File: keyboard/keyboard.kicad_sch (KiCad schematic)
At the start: 132 parts, among them SW1 MX_SW_HS, SW10 MX_SW_HS, SW11 MX_SW_HS, SW12 MX_SW_HS, SW13 MX_SW_HS, SW14 MX_SW_HS, SW15 MX_SW_HS, SW16 MX_SW_HS, SW17 MX_SW_HS, SW18 MX_SW_HS, SW19 MX_SW_HS, SW2 MX_SW_HS, SW20 MX_SW_HS, SW21 MX_SW_HS, SW22 MX_SW_HS, SW23 MX_SW_HS, SW24 MX_SW_HS, SW25 MX_SW_HS, SW26 MX_SW_HS, SW27 MX_SW_HS, SW28 MX_SW_HS, SW29 MX_SW_HS, SW3 MX_SW_HS, SW30 MX_SW_HS, SW31 MX_SW_HS, SW32 MX_SW_HS, SW33 MX_SW_HS, SW34 MX_SW_HS, SW35 MX_SW_HS, SW36 MX_SW_HS, SW37 MX_SW_HS, SW38 MX_SW_HS, SW39 MX_SW_HS, SW4 MX_SW_HS, SW40 MX_SW_HS, SW41 MX_SW_HS, SW42 MX_SW_HS, SW43 MX_SW_HS, SW44 MX_SW_HS, SW45 MX_SW_HS, SW46 MX_SW_HS, SW47 MX_SW_HS, SW48 MX_SW_HS, SW49 MX_SW_HS, SW5 MX_SW_HS, SW50 MX_SW_HS, SW51 MX_SW_HS, SW52 MX_SW_HS, SW53 MX_SW_HS, SW54 MX_SW_HS, SW55 MX_SW_HS, SW56 MX_SW_HS, SW57 MX_SW_HS, SW58 MX_SW_HS, SW59 MX_SW_HS, SW6 MX_SW_HS, SW60 MX_SW_HS, SW61 MX_SW_HS, SW62 MX_SW_HS, SW63 MX_SW_HS, SW64 MX_SW_HS, SW7 MX_SW_HS, SW8 MX_SW_HS, SW9 MX_SW_HS, U1 ProMicro

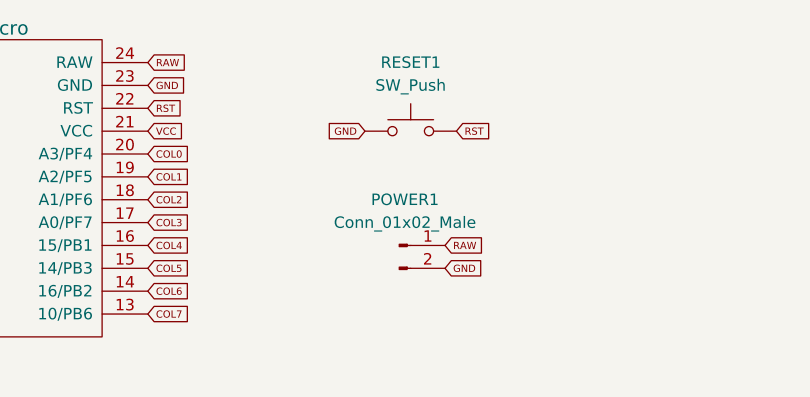
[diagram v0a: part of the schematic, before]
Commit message: Add the connector for the power switch and the holes for the broaching nuts
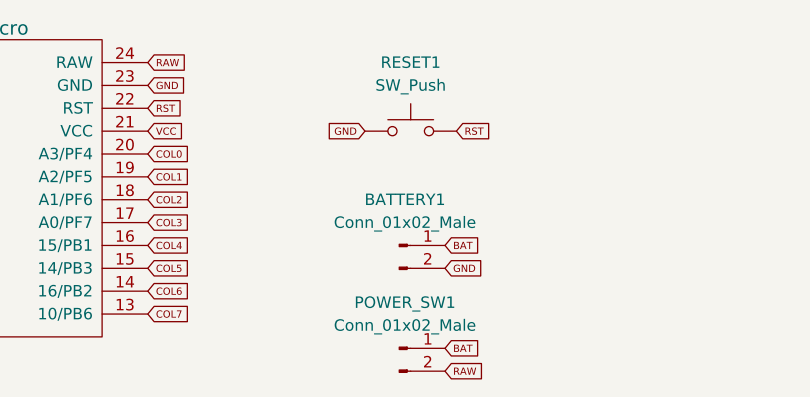
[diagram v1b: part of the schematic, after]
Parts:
- added POWER_SW1: Conn_01x02_Male, symbol Connector:Conn_01x02_Male
- renumbered POWER1 to BATTERY1
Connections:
- net RAW: now also POWER_SW1.2 (Pin_2); no longer BATTERY1.1 (Pin_1)
- new net BAT: BATTERY1.1 (Pin_1), POWER_SW1.1 (Pin_1)
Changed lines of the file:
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@@
+    )
+  )
+  (global_label "BAT" (shape input) (at 100.33 181.61 0) (fields_autoplaced)
+    (effects (font (size 0.8 0.8)) (justify left))
+    (property "Intersheet References" "${INTERSHEET_REFS}" (id 0) (at 103.9452 181.56 0)
+      (effects (font (size 0.8 0.8)) (justify left) hide)
     )
   )
@@
     )
   )
+  (global_label "RAW" (shape input) (at 100.33 184.15 0) (fields_autoplaced)
+    (effects (font (size 0.8 0.8)) (justify left))
+    (property "Intersheet References" "${INTERSHEET_REFS}" (id 0) (at 104.25 184.1 0)
+      (effects (font (size 0.8 0.8)) (justify left) hide)
+    )
+  )
   (global_label "ROW7" (shape input) (at 223.52 95.25 180) (fields_autoplaced)
     (effects (font (size 0.6 0.6)) (justify right))
@@
     )
   )
-  (global_label "RAW" (shape input) (at 100.33 170.18 0) (fields_autoplaced)
+  (global_label "BAT" (shape input) (at 100.33 170.18 0) (fields_autoplaced)
     (effects (font (size 0.8 0.8)) (justify left))
-    (property "Intersheet References" "${INTERSHEET_REFS}" (id 0) (at 104.25 170.13 0)
+    (property "Intersheet References" "${INTERSHEET_REFS}" (id 0) (at 103.9452 170.13 0)
       (effects (font (size 0.8 0.8)) (justify left) hide)
     )
@@
   (symbol (lib_id "Connector:Conn_01x02_Male") (at 95.25 170.18 0) (unit 1)
     (in_bom yes) (on_board yes) (fields_autoplaced)
-    (property "Reference" "POWER1" (id 0) (at 95.885 165.1 0))
+    (property "Reference" "BATTERY1" (id 0) (at 95.885 165.1 0))
     (property "Value" "Conn_01x02_Male" (id 1) (at 95.885 167.64 0))
     (property "Footprint" "" (id 2) (at 95.25 170.18 0)
@@
     (pin "2")
   )
+  (symbol (lib_id "Connector:Conn_01x02_Male") (at 95.25 181.61 0) (unit 1)
+    (in_bom yes) (on_board yes) (fields_autoplaced)
+    (property "Reference" "POWER_SW1" (id 0) (at 95.885 176.53 0))
+    (property "Value" "Conn_01x02_Male" (id 1) (at 95.885 179.07 0))
+    (property "Footprint" "" (id 2) (at 95.25 181.61 0)
+      (effects (font (size 1.27 1.27)) hide)
+    )
+    (property "Datasheet" "~" (id 3) (at 95.25 181.61 0)
+      (effects (font (size 1.27 1.27)) hide)
+    )
+    (pin "1")
+    (pin "2")
+  )
   (symbol (lib_id "Diode:1N4148") (at 76.2 95.25 0) (unit 1)
     (in_bom yes) (on_board yes) (fields_autoplaced)
@@
   )
   (symbol_instances
+    (path "/0ea7d412-6277-4227-b71e-6e4e29ffda6b"
+      (reference "BATTERY1") (unit 1) (value "Conn_01x02_Male") (footprint "Connector_PinHeader_2.54mm:PinHeader_1x02_P2.54mm_Vertical")
+    )
     (path "/6e969bfa-28c9-4212-88d0-f22e18a188be"
       (reference "D1") (unit 1) (value "1N4148") (footprint "Diode_THT:D_DO-35_SOD27_P7.62mm_Horizontal")
@@
       (reference "D64") (unit 1) (value "1N4148") (footprint "Diode_THT:D_DO-35_SOD27_P7.62mm_Horizontal")
     )
-    (path "/0ea7d412-6277-4227-b71e-6e4e29ffda6b"
-      (reference "POWER1") (unit 1) (value "Conn_01x02_Male") (footprint "Connector_PinHeader_2.54mm:PinHeader_1x02_P2.54mm_Vertical")
+    (path "/eda49190-6b3d-4bb1-b40a-0d620c2aa1aa"
+      (reference "POWER_SW1") (unit 1) (value "Conn_01x02_Male") (footprint "Connector_PinHeader_2.54mm:PinHeader_1x02_P2.54mm_Horizontal")
     )
     (path "/69aaefbf-88d4-415d-ad96-2a6ff3ee3a2f"

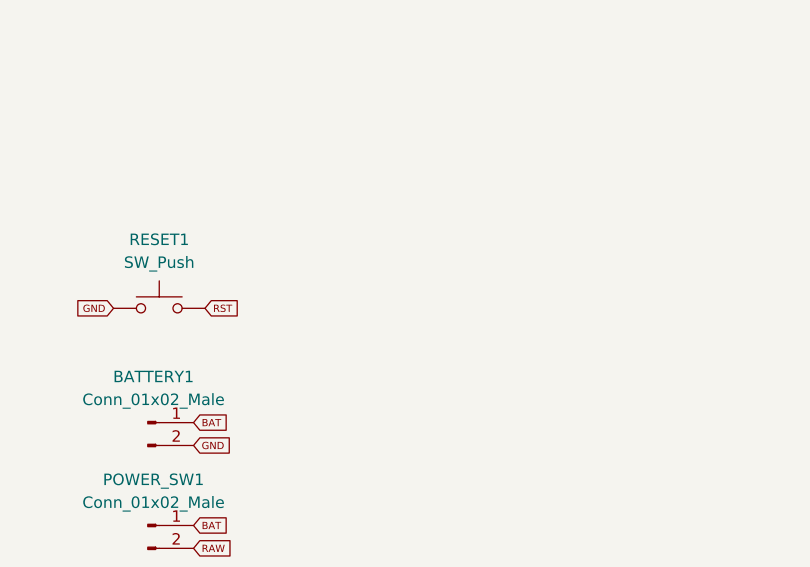
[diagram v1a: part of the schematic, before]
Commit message: Add the display adapter
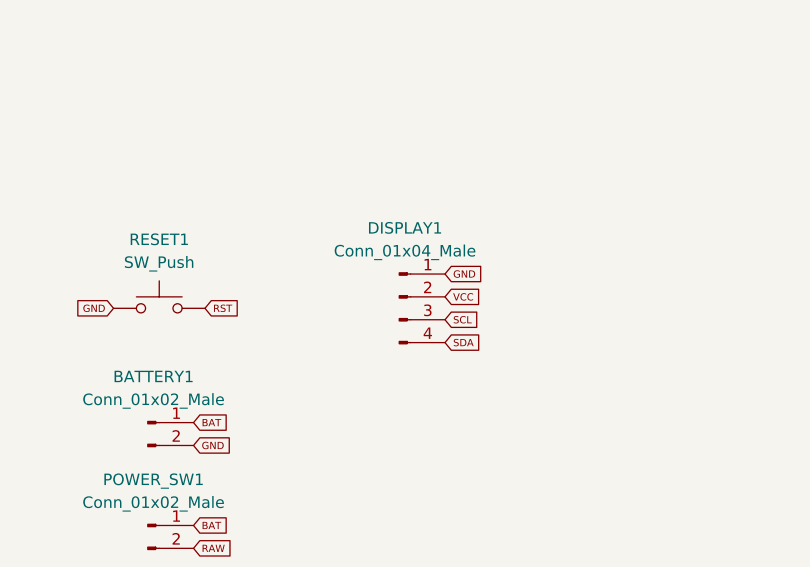
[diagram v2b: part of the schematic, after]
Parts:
- added DISPLAY1: Conn_01x04_Male, Connector_PinHeader_2.54mm:PinHeader_1x04_P2.54mm_Vertical, symbol Connector:Conn_01x04_Male
- BATTERY1: footprint (none) -> Connector_PinHeader_2.54mm:PinHeader_1x02_P2.54mm_Vertical
- POWER_SW1: footprint (none) -> Connector_PinHeader_2.54mm:PinHeader_1x02_P2.54mm_Horizontal
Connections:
- net GND: now also DISPLAY1.1 (Pin_1)
- net SCL: now also DISPLAY1.3 (Pin_3)
- net SDA: now also DISPLAY1.4 (Pin_4)
- net VCC: now also DISPLAY1.2 (Pin_2)
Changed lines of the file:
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@@
+    )
+  )
+  (global_label "SDA" (shape input) (at 128.27 161.29 0) (fields_autoplaced)
+    (effects (font (size 0.8 0.8)) (justify left))
+    (property "Intersheet References" "${INTERSHEET_REFS}" (id 0) (at 132.0376 161.24 0)
+      (effects (font (size 0.8 0.8)) (justify left) hide)
     )
   )
@@
     )
   )
+  (global_label "VCC" (shape input) (at 128.27 156.21 0) (fields_autoplaced)
+    (effects (font (size 0.8 0.8)) (justify left))
+    (property "Intersheet References" "${INTERSHEET_REFS}" (id 0) (at 132.0757 156.16 0)
+      (effects (font (size 0.8 0.8)) (justify left) hide)
+    )
+  )
   (global_label "COL0" (shape input) (at 29.21 43.18 180) (fields_autoplaced)
     (effects (font (size 0.6 0.6)) (justify right))
@@
     )
   )
+  (global_label "GND" (shape input) (at 128.27 153.67 0) (fields_autoplaced)
+    (effects (font (size 0.8 0.8)) (justify left))
+    (property "Intersheet References" "${INTERSHEET_REFS}" (id 0) (at 132.2281 153.62 0)
+      (effects (font (size 0.8 0.8)) (justify left) hide)
+    )
+  )
   (global_label "COL7" (shape input) (at 223.52 43.18 180) (fields_autoplaced)
     (effects (font (size 0.6 0.6)) (justify right))
@@
     (property "Intersheet References" "${INTERSHEET_REFS}" (id 0) (at 111.9443 95.2125 0)
       (effects (font (size 0.6 0.6)) (justify right) hide)
+    )
+  )
+  (global_label "SCL" (shape input) (at 128.27 158.75 0) (fields_autoplaced)
+    (effects (font (size 0.8 0.8)) (justify left))
+    (property "Intersheet References" "${INTERSHEET_REFS}" (id 0) (at 131.9995 158.7 0)
+      (effects (font (size 0.8 0.8)) (justify left) hide)
     )
   )
@@
     (property "Reference" "BATTERY1" (id 0) (at 95.885 165.1 0))
     (property "Value" "Conn_01x02_Male" (id 1) (at 95.885 167.64 0))
-    (property "Footprint" "" (id 2) (at 95.25 170.18 0)
+    (property "Footprint" "Connector_PinHeader_2.54mm:PinHeader_1x02_P2.54mm_Vertical" (id 2) (at 95.25 170.18 0)
       (effects (font (size 1.27 1.27)) hide)
     )
@@
     (pin "1")
     (pin "2")
+  )
+  (symbol (lib_id "Connector:Conn_01x04_Male") (at 123.19 156.21 0) (unit 1)
+    (in_bom yes) (on_board yes) (fields_autoplaced)
+    (property "Reference" "DISPLAY1" (id 0) (at 123.825 148.59 0))
+    (property "Value" "Conn_01x04_Male" (id 1) (at 123.825 151.13 0))
+    (property "Footprint" "Connector_PinHeader_2.54mm:PinHeader_1x04_P2.54mm_Vertical" (id 2) (at 123.19 156.21 0)
+      (effects (font (size 1.27 1.27)) hide)
+    )
+    (property "Datasheet" "~" (id 3) (at 123.19 156.21 0)
+      (effects (font (size 1.27 1.27)) hide)
+    )
+    (pin "1")
+    (pin "2")
+    (pin "3")
+    (pin "4")
   )
   (symbol (lib_id "Diode:1N4148") (at 54.61 67.31 0) (unit 1)
@@
     (property "Reference" "POWER_SW1" (id 0) (at 95.885 176.53 0))
     (property "Value" "Conn_01x02_Male" (id 1) (at 95.885 179.07 0))
-    (property "Footprint" "" (id 2) (at 95.25 181.61 0)
+    (property "Footprint" "Connector_PinHeader_2.54mm:PinHeader_1x02_P2.54mm_Horizontal" (id 2) (at 95.25 181.61 0)
       (effects (font (size 1.27 1.27)) hide)
     )
@@
       (reference "D64") (unit 1) (value "1N4148") (footprint "Diode_THT:D_DO-35_SOD27_P7.62mm_Horizontal")
     )
+    (path "/3ca855ba-d11e-499d-8a9f-fe87acf95d55"
+      (reference "DISPLAY1") (unit 1) (value "Conn_01x04_Male") (footprint "Connector_PinHeader_2.54mm:PinHeader_1x04_P2.54mm_Vertical")
+    )
     (path "/eda49190-6b3d-4bb1-b40a-0d620c2aa1aa"
